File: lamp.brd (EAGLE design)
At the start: 37.4 x 50.6 mm, 15 parts, among them IC1 LM358D, T2 TIP32C

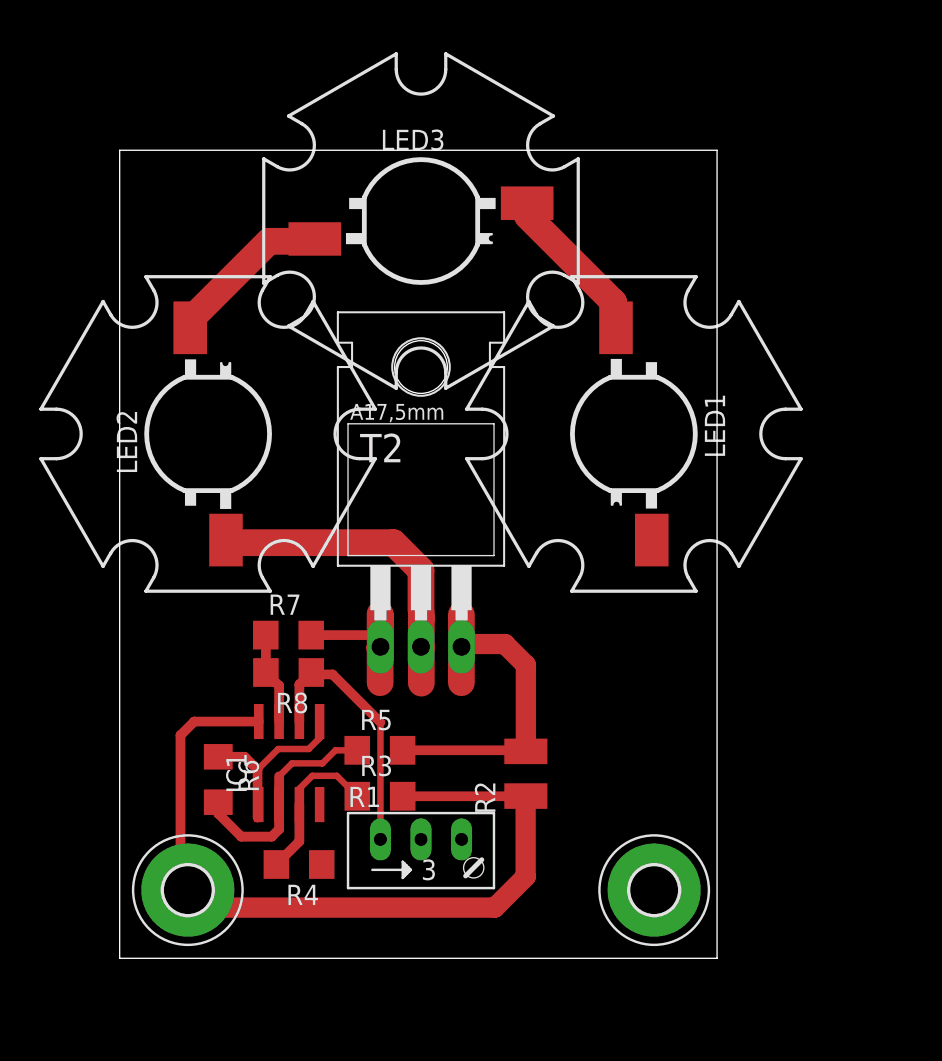
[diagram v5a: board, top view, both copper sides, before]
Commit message: Added a power switch.
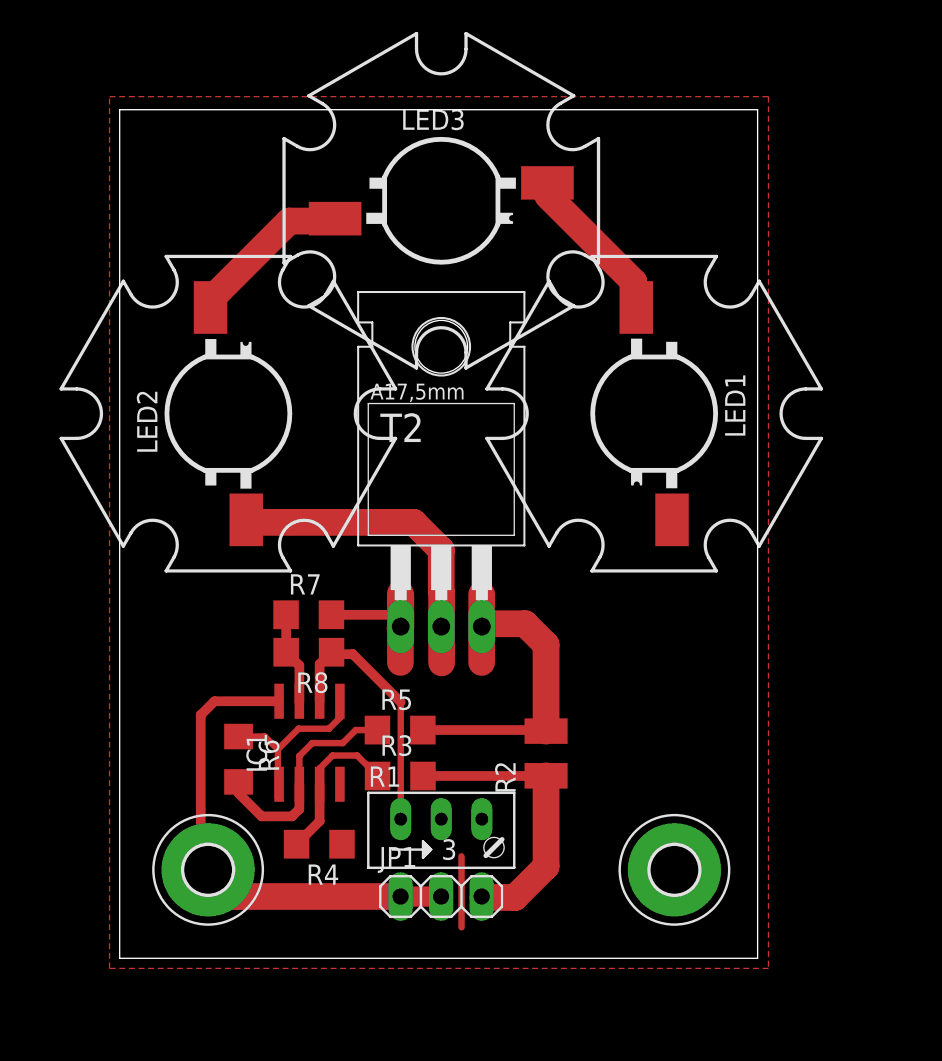
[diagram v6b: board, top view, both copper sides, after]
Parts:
- added JP1: (no value), pinhead:1X03
- moved LED1 1.80 mm to (33.5, 34.1)
- moved LED2 1.80 mm to (6.81, 34.1)
- moved LED3 1.80 mm to (20.1, 47.5)
- moved R7 1.80 mm to (11.8, 21.5)
- moved R2 1.80 mm to (26.7, 12.8)
- moved R6 1.80 mm to (7.45, 12.5)
- moved R8 1.80 mm to (11.9, 19.2)
- moved VCC 1.80 mm to (5.54, 5.54)
- moved IC1 1.80 mm to (11.9, 13.5)
- moved R1 1.80 mm to (20.1, 8.08)
- moved R3 1.80 mm to (17.6, 11.4)
- moved R4 1.80 mm to (12.5, 7.15)
- moved R5 1.80 mm to (17.6, 14.3)
- moved T2 1.80 mm to (20.1, 27.1)
- moved GND 1.80 mm to (34.7, 5.54)
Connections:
- new net N$24: JP1.3, R2.1, R3.2
- net VCC: now also JP1.1, JP1.2; no longer R2.1, R3.2
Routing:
- net VCC: track 53.5 -> 30.4 mm
- net N$24: track 0.00 -> 18.3 mm
- net GND: track 0.00 -> 4.44 mm
- added copper zone on layer 1, net GND
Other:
- board size 37.4 x 50.6 mm -> 40 x 53.2 mm

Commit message: Added another mounting hole & removed the potentiometer.
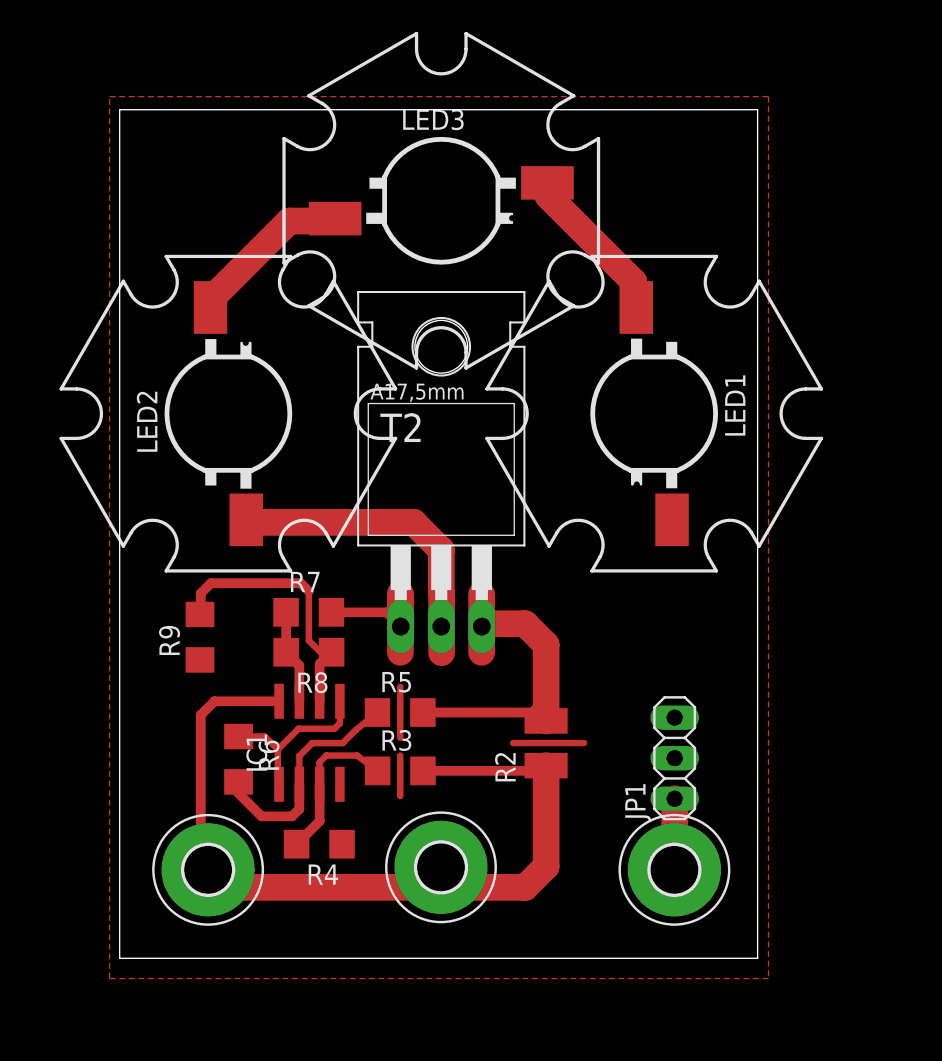
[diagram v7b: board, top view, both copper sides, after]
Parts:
- removed R1: 10k, pot:RJ9W
- added R9: (no value), resistor:R1206
- added VCC1: MOUNT-PAD-ROUND3.0, holes:3,0-PAD
- R8: value 47k -> 470k
- moved JP1 17.0 mm to (34.8, 12.5), turned to 90 degrees
- moved R5 1.10 mm to (17.6, 15.4)
- moved R2 0.63 mm to (26.7, 13.5)
- moved R3 0.32 mm to (17.6, 11.7)
- moved R7 0.15 mm to (11.8, 21.7)
- renumbered GND to GROUND
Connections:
- removed net N$24: JP1.3, R2.1, R3.2
- new net N$25: GROUND.B3,0, JP1.1
- net GND: now also JP1.2, JP1.3, R9.1; no longer GROUND.B3,0, R1.S
- net N$10: now also R9.2; no longer R1.E
- net VCC: now also R2.1, R3.2, VCC1.B3,0; no longer JP1.1, JP1.2
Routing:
- net VCC: track 30.4 -> 51.9 mm
- net N$24: track 18.3 -> 0.00 mm
- net GND: track 4.44 -> 10.2 mm
- net N$25: track 0.00 -> 4.46 mm
- net N$2: track 17.8 -> 18.9 mm
- net N$23: track 4.27 -> 3.64 mm
- net N$22: track 4.35 -> 3.71 mm
- net N$17: track 4.32 -> 3.69 mm
